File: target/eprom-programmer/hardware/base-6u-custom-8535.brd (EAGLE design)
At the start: 68.6 x 61 mm, 20 parts, among them IC1 MEGA8535-P

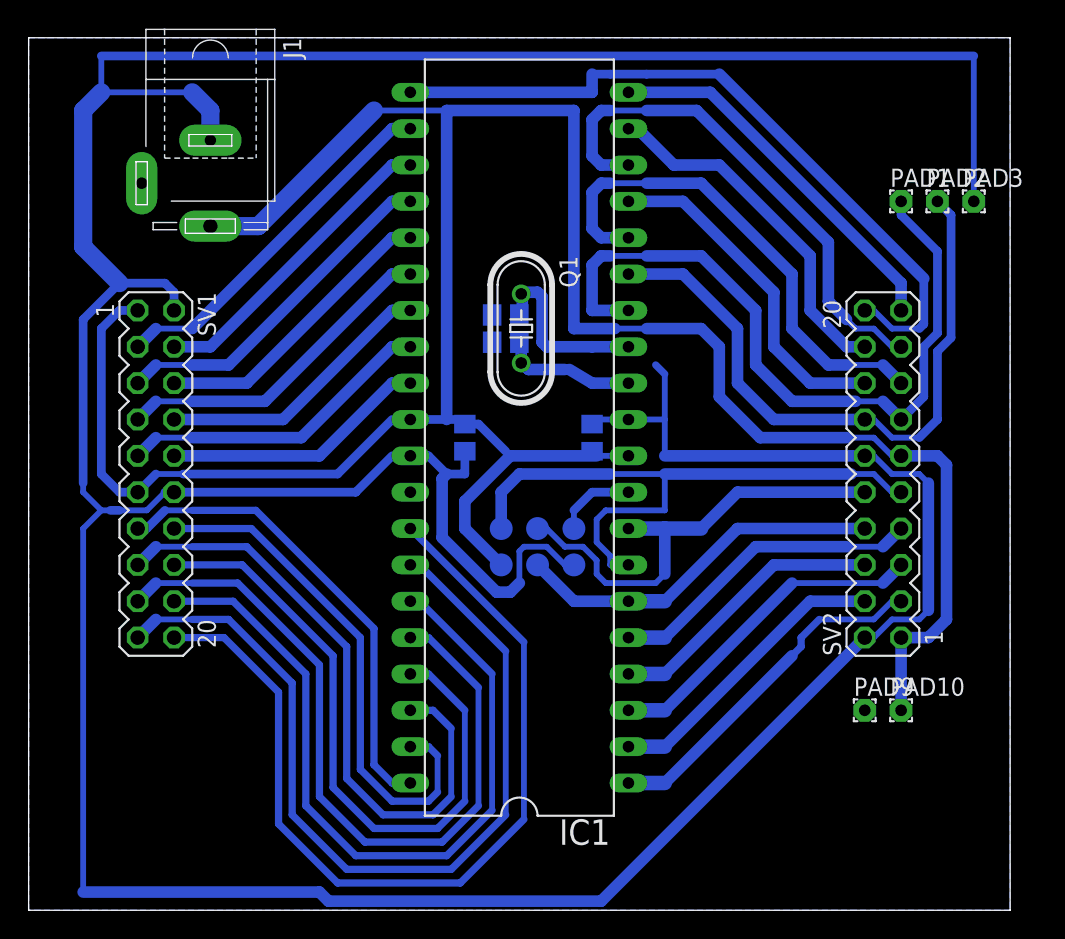
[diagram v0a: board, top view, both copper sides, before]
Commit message: eprom-programmer: hardware
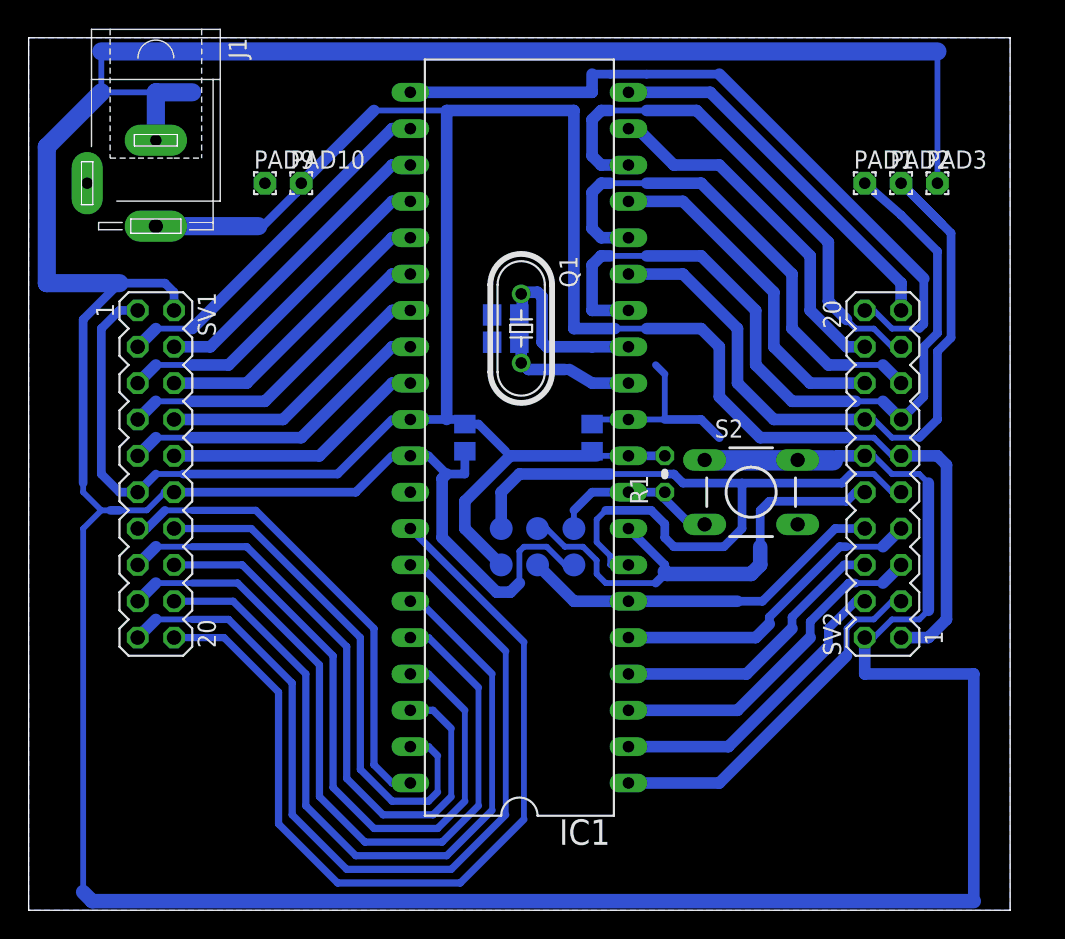
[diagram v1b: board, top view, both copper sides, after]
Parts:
- added R1: (no value), rcl:0204V
- added S2: DTS-6, switch-tact:DTS-6
- moved PAD10 55.8 mm to (35.6, 61.0)
- moved PAD9 55.8 mm to (33.0, 61.0)
- moved J1 3.81 mm to (25.4, 61.0)
- moved PAD2 2.84 mm to (77.5, 61.0)
- moved PAD1 2.84 mm to (74.9, 61.0)
- moved PAD3 2.84 mm to (80.0, 61.0)
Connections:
- net GND: now also S2.1
- net RESET: now also R1.1, S2.3
- net VCC: now also R1.2
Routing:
- net GND: track 304.0 -> 331.2 mm
- net PB6_MISO: track 43.9 -> 52.6 mm
- net RESET: track 5.61 -> 12.2 mm
- net PD1: track 45.6 -> 51.5 mm
- net PD0: track 51.9 -> 54.3 mm
- net PB7_SCK: track 32.0 -> 34.2 mm
- net VCC: track 181.4 -> 182.8 mm
- net PB1: track 20.7 -> 21.5 mm
- net PB0: track 24.7 -> 25.4 mm
- net PB2: track 23.3 -> 23.9 mm
